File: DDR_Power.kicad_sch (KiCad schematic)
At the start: 15 parts, among them U2 Micron DDR4 MT40A512M16TB, U6 PT5108E23E

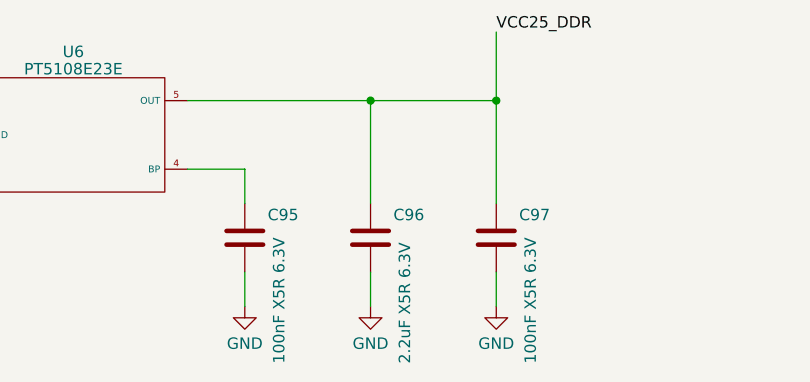
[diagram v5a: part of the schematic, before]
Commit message: updated LCSC selection of capacitors
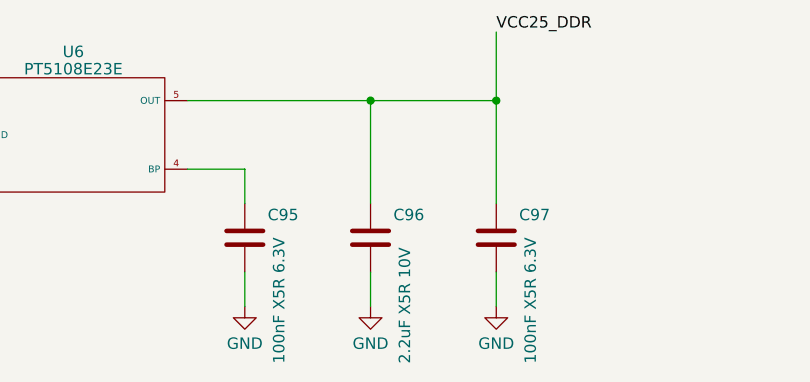
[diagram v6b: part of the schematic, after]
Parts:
- C90, C93: LCSC (none) -> C91601; Model (none) -> GCM155R71H103KA55D; Vendor (none) -> muRata(村田)
- C91: Model (none) -> GRM155R61A225KE01D; Vendor (none) -> muRata(村田)
- C92, C94: LCSC (none) -> C77018; Model (none) -> GRM155R71H102KA01D
- C96: value 2.2uF X5R 6.3V -> 2.2uF X5R 10V; Model (none) -> GRM155R61A225KE01D; Vendor (none) -> muRata(村田)
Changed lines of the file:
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@@
+      (effects (font (size 1.27 1.27)) hide)
+    )
+    (property "Description" "容值: 1nF 精度: ±10% 额定电压: 50V 材质(温度系数): X7R 材质:X7R" (at 81.28 77.47 0)
+      (effects (font (size 1.27 1.27)) hide)
+    )
+    (property "LCSC" "C77018" (at 81.28 77.47 0)
+      (effects (font (size 1.27 1.27)) hide)
+    )
+    (property "Model" "GRM155R71H102KA01D" (at 81.28 77.47 0)
       (effects (font (size 1.27 1.27)) hide)
     )
@@
     )
     (property "Datasheet" "~" (at 46.99 77.47 0)
+      (effects (font (size 1.27 1.27)) hide)
+    )
+    (property "Description" "容值: 10nF 精度: ±10% 额定电压: 50V 材质(温度系数): X7R 材质:X7R" (at 46.99 77.47 0)
+      (effects (font (size 1.27 1.27)) hide)
+    )
+    (property "LCSC" "C91601" (at 46.99 77.47 0)
+      (effects (font (size 1.27 1.27)) hide)
+    )
+    (property "Model" "GCM155R71H103KA55D" (at 46.99 77.47 0)
+      (effects (font (size 1.27 1.27)) hide)
+    )
+    (property "Vendor" "muRata(村田)" (at 46.99 77.47 0)
       (effects (font (size 1.27 1.27)) hide)
     )
@@
       (effects (font (size 1.27 1.27)) hide)
     )
+    (property "Description" "容值: 2.2uF 精度: ±10% 额定电压: 10V 材质(温度系数): X5R" (at 46.99 142.24 0)
+      (effects (font (size 1.27 1.27)) hide)
+    )
+    (property "Model" "GRM155R61A225KE01D" (at 46.99 142.24 0)
+      (effects (font (size 1.27 1.27)) hide)
+    )
+    (property "Vendor" "muRata(村田)" (at 46.99 142.24 0)
+      (effects (font (size 1.27 1.27)) hide)
+    )
     (pin "1")
     (pin "2")
@@
       (effects (font (size 1.27 1.27)) hide)
     )
+    (property "Description" "容值: 10nF 精度: ±10% 额定电压: 50V 材质(温度系数): X7R 材质:X7R" (at 69.85 77.47 0)
+      (effects (font (size 1.27 1.27)) hide)
+    )
+    (property "LCSC" "C91601" (at 69.85 77.47 0)
+      (effects (font (size 1.27 1.27)) hide)
+    )
+    (property "Model" "GCM155R71H103KA55D" (at 69.85 77.47 0)
+      (effects (font (size 1.27 1.27)) hide)
+    )
+    (property "Vendor" "muRata(村田)" (at 69.85 77.47 0)
+      (effects (font (size 1.27 1.27)) hide)
+    )
     (pin "1")
     (pin "2")
@@
       (effects (font (size 1.27 1.27)) hide)
     )
+    (property "Description" "容值: 1nF 精度: ±10% 额定电压: 50V 材质(温度系数): X7R 材质:X7R" (at 58.42 77.47 0)
+      (effects (font (size 1.27 1.27)) hide)
+    )
+    (property "LCSC" "C77018" (at 58.42 77.47 0)
+      (effects (font (size 1.27 1.27)) hide)
+    )
+    (property "Model" "GRM155R71H102KA01D" (at 58.42 77.47 0)
+      (effects (font (size 1.27 1.27)) hide)
+    )
     (pin "1")
     (pin "2")
@@
       (effects (font (size 1.27 1.27)) (justify left))
     )
-    (property "Value" "2.2uF X5R 6.3V" (at 139.7 166.37 90)
+    (property "Value" "2.2uF X5R 10V" (at 139.7 166.37 90)
       (effects (font (size 1.27 1.27)) (justify left))
     )
@@
       (effects (font (size 1.27 1.27)) hide)
     )
+    (property "Description" "容值: 2.2uF 精度: ±10% 额定电压: 10V 材质(温度系数): X5R" (at 135.89 152.4 0)
+      (effects (font (size 1.27 1.27)) hide)
+    )
+    (property "Model" "GRM155R61A225KE01D" (at 135.89 152.4 0)
+      (effects (font (size 1.27 1.27)) hide)
+    )
+    (property "Vendor" "muRata(村田)" (at 135.89 152.4 0)
+      (effects (font (size 1.27 1.27)) hide)
+    )

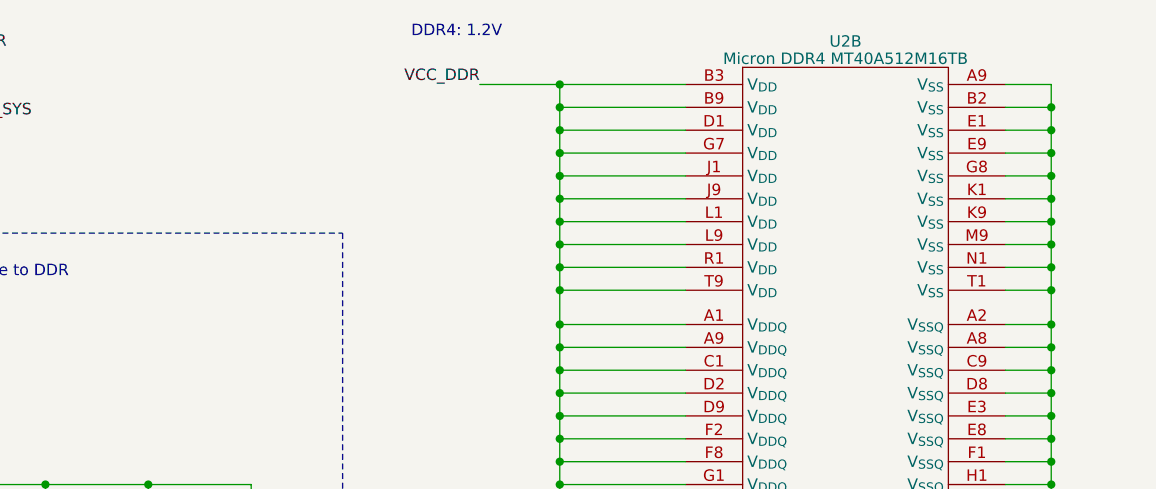
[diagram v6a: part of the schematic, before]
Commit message: layout SoC Power and DDR capacitors
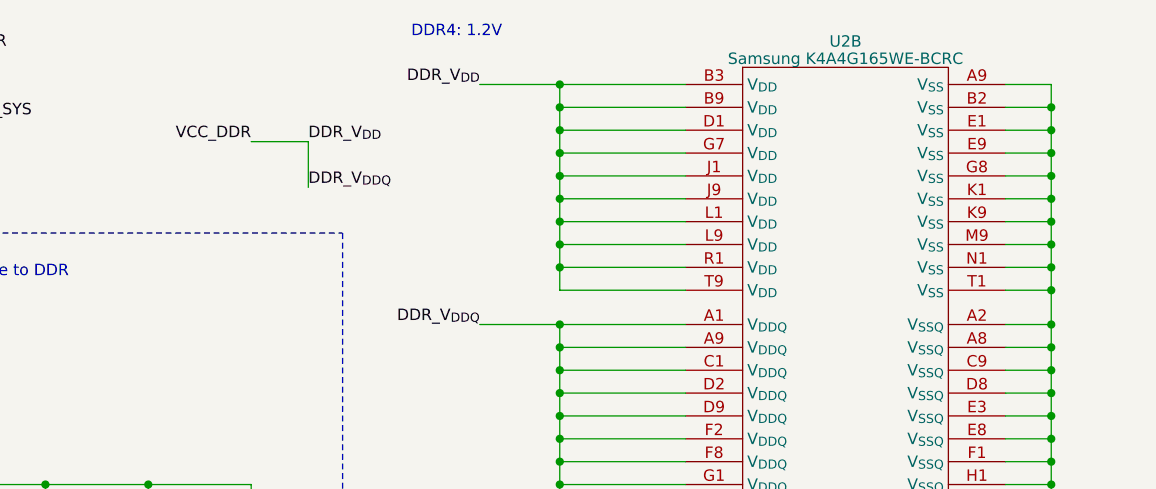
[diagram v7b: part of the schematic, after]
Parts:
- C95, C97: LCSC C76934 -> C76928; Model GRM033R61A104KE15D -> GRM033R60J104KE19D
- U2: value Micron DDR4 MT40A512M16TB -> Samsung K4A4G165WE-BCRC; LCSC (none) -> C2803250; Model (none) -> K4A4G165WE-BCRC; Vendor (none) -> SAMSUNG(三星半导体)
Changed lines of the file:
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@@
   (junction (at 170.18 57.15) (diameter 0) (color 0 0 0 0)
   )
-  (junction (at 115.57 48.26) (diameter 0) (color 0 0 0 0)
-  )
   (junction (at 115.57 35.56) (diameter 0) (color 0 0 0 0)
   )
@@
   (junction (at 115.57 59.69) (diameter 0) (color 0 0 0 0)
   )
+  (junction (at 115.57 62.23) (diameter 0) (color 0 0 0 0)
+  )
+  (junction (at 170.18 52.07) (diameter 0) (color 0 0 0 0)
+  )
   (junction (at 115.57 52.07) (diameter 0) (color 0 0 0 0)
   )
-  (junction (at 115.57 62.23) (diameter 0) (color 0 0 0 0)
-  )
-  (junction (at 170.18 52.07) (diameter 0) (color 0 0 0 0)
-  )
   (junction (at 115.57 54.61) (diameter 0) (color 0 0 0 0)
   )
@@
     (stroke (width 0) (type default))
   )
+  (wire (pts (xy 81.28 31.75) (xy 87.63 31.75))
+    (stroke (width 0) (type default))
+  )
   (wire (pts (xy 115.57 77.47) (xy 115.57 74.93))
     (stroke (width 0) (type default))
@@
     (stroke (width 0) (type default))
   )
+  (wire (pts (xy 87.63 31.75) (xy 87.63 36.83))
+    (stroke (width 0) (type default))
+  )
   (wire (pts (xy 165.1 67.31) (xy 170.18 67.31))
     (stroke (width 0) (type default))
@@
     (stroke (width 0) (type default))
   )
-  (wire (pts (xy 115.57 48.26) (xy 115.57 52.07))
-    (stroke (width 0) (type default))
-  )
   (wire (pts (xy 115.57 38.1) (xy 115.57 40.64))
     (stroke (width 0) (type default))
@@
   )
   (wire (pts (xy 200.66 124.46) (xy 208.28 124.46))
+    (stroke (width 0) (type default))
+  )
+  (wire (pts (xy 106.68 52.07) (xy 115.57 52.07))
     (stroke (width 0) (type default))
   )
@@
     (effects (font (size 1.27 1.27)) (justify left bottom))
   )
+  (label "VCC_DDR" (at 81.28 31.75 180) (fields_autoplaced)
+    (effects (font (size 1.27 1.27)) (justify right bottom))
+  )
   (label "DDR_VREFCA" (at 179.07 82.55 0) (fields_autoplaced)
     (effects (font (size 1.27 1.27)) (justify left bottom))
@@
     (effects (font (size 1.27 1.27)) (justify right bottom))
   )
+  (label "DDR_V_{DDQ}" (at 106.68 52.07 180) (fields_autoplaced)
+    (effects (font (size 1.27 1.27)) (justify right bottom))
+  )
+  (label "DDR_V_{DD}" (at 106.68 25.4 180) (fields_autoplaced)
+    (effects (font (size 1.27 1.27)) (justify right bottom))
+  )
+  (label "DDR_V_{DD}" (at 87.63 31.75 0) (fields_autoplaced)
+    (effects (font (size 1.27 1.27)) (justify left bottom))
+  )
+  (label "DDR_V_{DDQ}" (at 87.63 36.83 0) (fields_autoplaced)
+    (effects (font (size 1.27 1.27)) (justify left bottom))
+  )
   (label "VCC25_DDR" (at 109.22 82.55 180) (fields_autoplaced)
-    (effects (font (size 1.27 1.27)) (justify right bottom))
-  )
-  (label "VCC_DDR" (at 106.68 25.4 180) (fields_autoplaced)
     (effects (font (size 1.27 1.27)) (justify right bottom))
   )
@@
       (effects (font (size 1.27 1.27)))
     )
-    (property "Value" "Micron DDR4 MT40A512M16TB" (at 147.32 22.5331 0)
+    (property "Value" "Samsung K4A4G165WE-BCRC" (at 147.32 22.5331 0)
       (effects (font (size 1.27 1.27)))
     )
@@
     )
     (property "Datasheet" "" (at 147.32 52.07 0)
+      (effects (font (size 1.27 1.27)) hide)
+    )
+    (property "Description" "存储器构架(格式): SDRAM DDR4 时钟频率(fc): 1200MHz 存储容量: 4Gbit 工作电压: 1.14V~1.26V 工作电" (at 147.32 52.07 0)
+      (effects (font (size 1.27 1.27)) hide)
+    )
+    (property "LCSC" "C2803250" (at 147.32 52.07 0)
+      (effects (font (size 1.27 1.27)) hide)
+    )
+    (property "Model" "K4A4G165WE-BCRC" (at 147.32 52.07 0)
+      (effects (font (size 1.27 1.27)) hide)
+    )
+    (property "Vendor" "SAMSUNG(三星半导体)" (at 147.32 52.07 0)
       (effects (font (size 1.27 1.27)) hide)
     )
@@
       (effects (font (size 1.27 1.27)) hide)
     )
-    (property "Description" "容值: 100nF 精度: ±10% 额定电压: 10V 材质(温度系数): X5R 材质:X5R" (at 149.86 152.4 0)
-      (effects (font (size 1.27 1.27)) hide)
-    )
-    (property "LCSC" "C76934" (at 149.86 152.4 0)
-      (effects (font (size 1.27 1.27)) hide)
-    )
-    (property "Model" "GRM033R61A104KE15D" (at 149.86 152.4 0)
+    (property "Description" "容值: 100nF 精度: ±10% 额定电压: 6.3V 材质(温度系数): X5R 材质:X5R" (at 149.86 152.4 0)
+      (effects (font (size 1.27 1.27)) hide)
+    )
+    (property "LCSC" "C76928" (at 149.86 152.4 0)
+      (effects (font (size 1.27 1.27)) hide)
+    )
+    (property "Model" "GRM033R60J104KE19D" (at 149.86 152.4 0)
       (effects (font (size 1.27 1.27)) hide)
     )
@@
       (effects (font (size 1.27 1.27)) hide)
     )
-    (property "Description" "容值: 100nF 精度: ±10% 额定电压: 10V 材质(温度系数): X5R 材质:X5R" (at 121.92 152.4 0)
-      (effects (font (size 1.27 1.27)) hide)
-    )
-    (property "LCSC" "C76934" (at 121.92 152.4 0)
-      (effects (font (size 1.27 1.27)) hide)
-    )
-    (property "Model" "GRM033R61A104KE15D" (at 121.92 152.4 0)
-      (effects (font (size 1.27 1.27)) hide)
-    )
+    (property "Description" "容值: 100nF 精度: ±10% 额定电压: 6.3V 材质(温度系数): X5R 材质:X5R" (at 121.92 152.4 0)
+      (effects (font (size 1.27 1.27)) hide)
+    )
+    (property "LCSC" "C76928" (at 121.92 152.4 0)
+      (effects (font (size 1.27 1.27)) hide)
+    )
+    (property "Model" "GRM033R60J104KE19D" (at 121.92 152.4 0)
+      (effects (font (size 1.27 1.27)) hide)
+    )
